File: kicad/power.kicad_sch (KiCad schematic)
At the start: 2 parts, among them J1 +5V IN

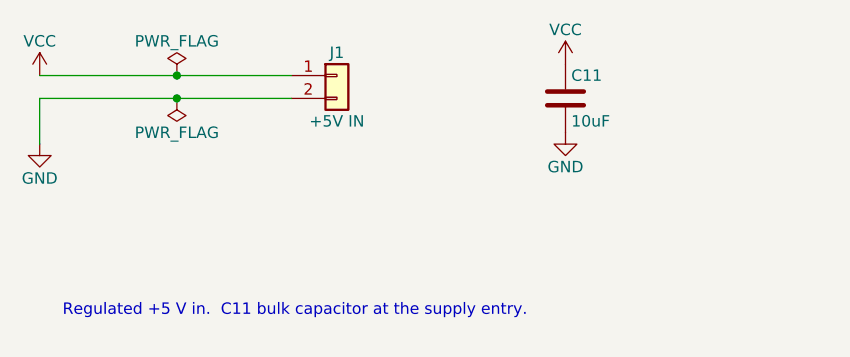
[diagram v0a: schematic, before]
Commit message: Update KiCad schematic to match the build as wired
- Remove video RAM (future expansion); GAL ~{VRAMCE} is NC and
  ~{WEGATE} goes only to the RAM
- VIA is a W65C22N6TPG-14: IRQB wired directly to ~{IRQ} (no diode)
- RDY and ~{NMI} tied directly to +5V; only reset and ~{IRQ} pull-ups
- ACIA clocked by a 1.8432 MHz DIP-8 oscillator on XTLI (EN high)
- Serial through a MAX232N to a female DB9 (pins 2, 3, 8, 5)
- VIA Port B drives eight LEDs with series resistors; Port A, CA/CB NC
- Drop per-chip decoupling; single 0.1uF electrolytic at the supply
- Unknown resistor values shown as '?'
- Update kicad/README.md and README.md accordingly

Co-Authored-By: Claude Opus 5.5 <noreply@anthropic.com>
Claude-Session: https://claude.ai/code/session_01GgTWzZQQJPzWrEMiSDZH6j
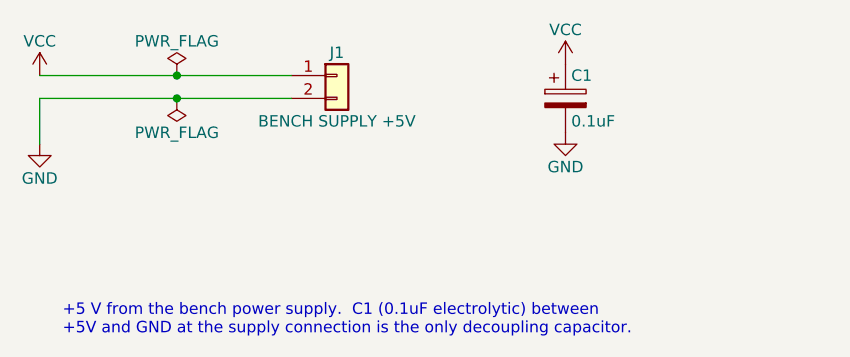
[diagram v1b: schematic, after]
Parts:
- removed C11: 10uF, symbol be6502:C
- added C1: 0.1uF, symbol be6502:C_Polarized
- J1: value +5V IN -> BENCH SUPPLY +5V
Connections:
- net GND: now also C1.2
- net VCC: now also C1.1
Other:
- note added: "+5 V from the bench power supply. C1 (0.1uF electrolytic) between +5V and GND at the supply connection is the only decoupling capacitor."
- note removed: "Regulated +5 V in. C11 bulk capacitor at the supply entry."

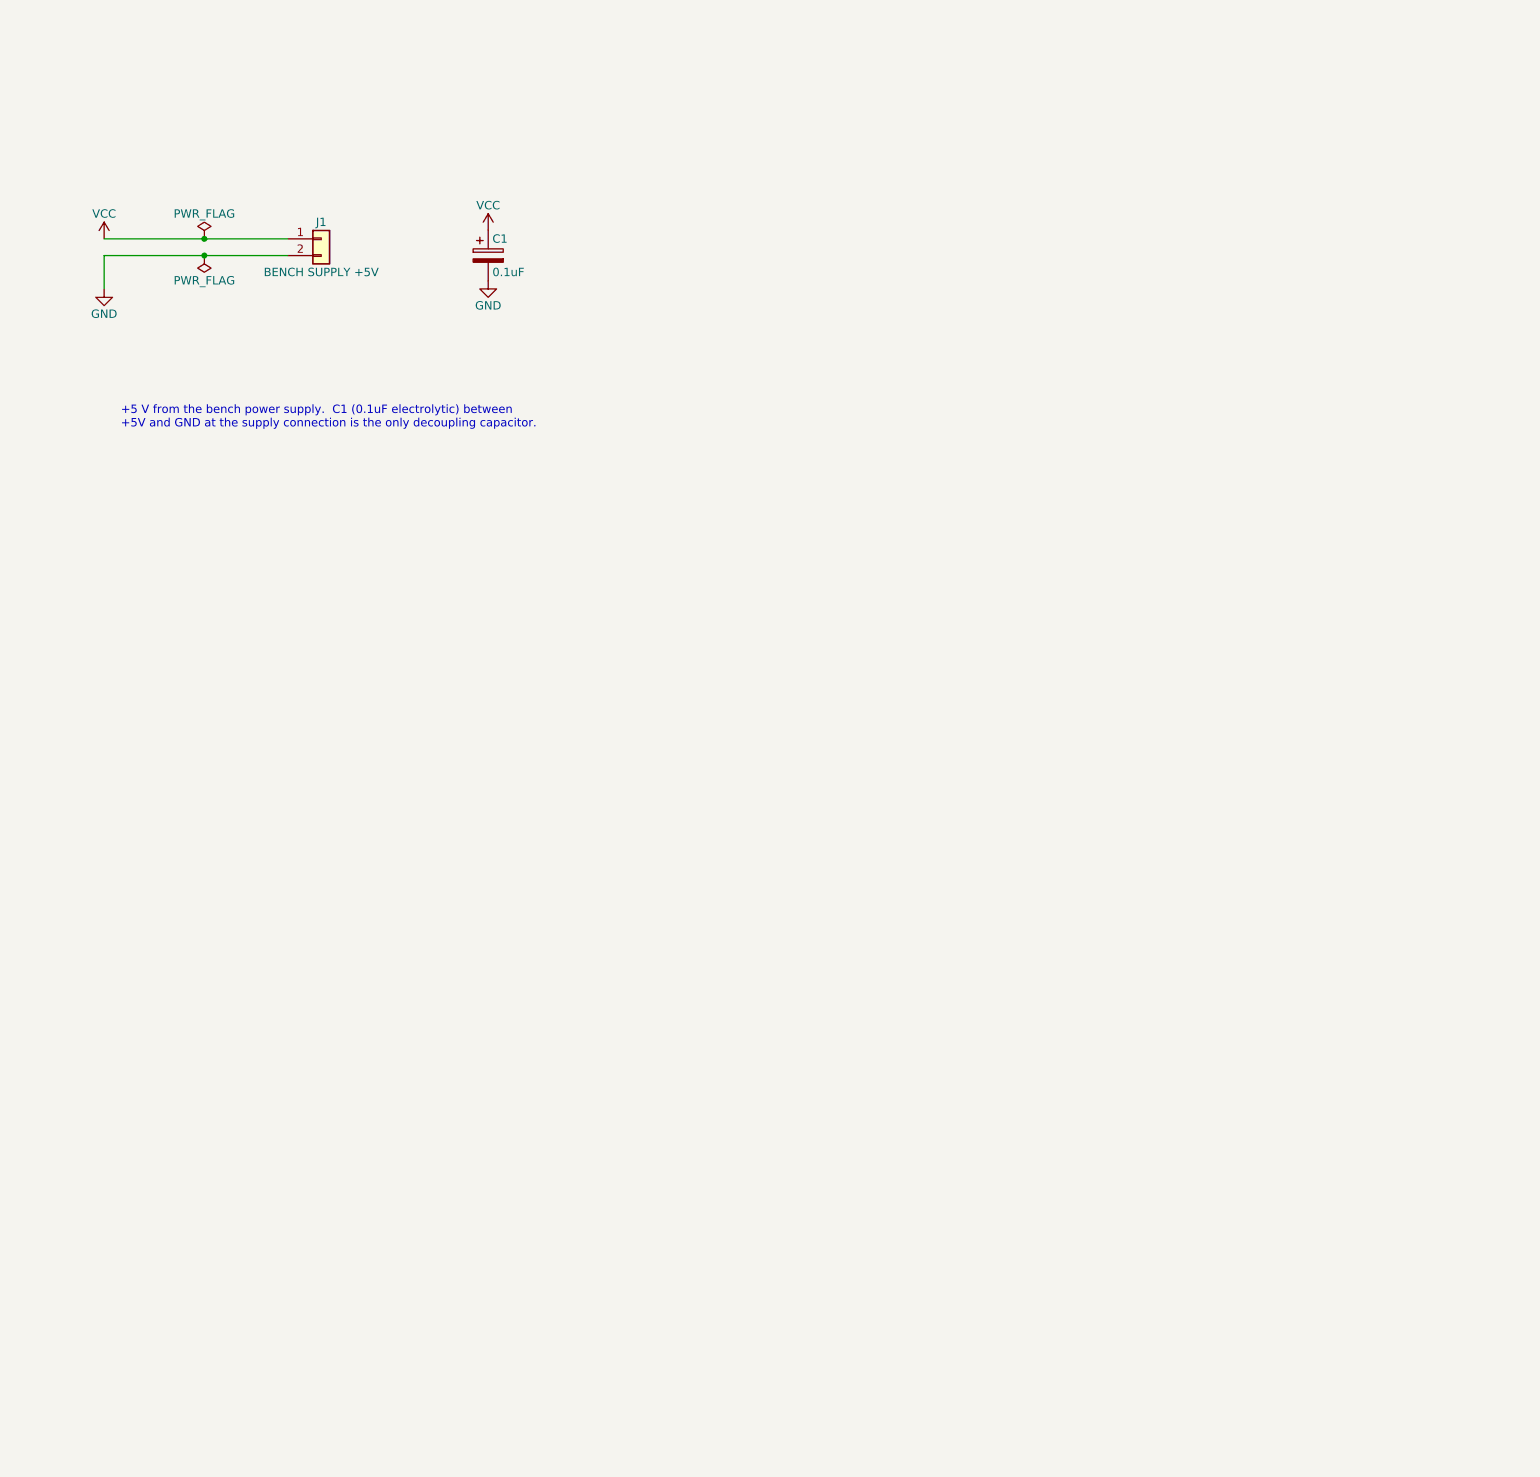
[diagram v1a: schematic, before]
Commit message: Schematic rev 2: prepare the design for a 4-layer PCB
Keeps the breadboard's parts and logic and adds what a board needs.

- RDY, NMI, ABORT and BE get 3.3k pull-ups instead of hard ties to +5V
  (RDY is bidirectional; WAI drives it low).
- VDA and VPA go to GAL pins 11 and 13. New pld/decode03.pld (816DEC03)
  qualifies /IOSEL with VDA + VPA so internal-operation cycles cannot
  read and clear ACIA/VIA registers. decode.pld (816DEC02) stays for the
  breadboard.
- PHI2 from the GAL can be routed through a 74ACT08 buffer via JP2
  (default: direct, as built). Timing in decode03.pld NOTE 8.
- Clock source jumper JP1 and external clock header J5.
- New power sheet: USB-C (power only) or bench terminal via JP4, power
  switch, polyfuse, P-FET reverse-polarity protection, 47uF bulk, power
  LED, and 100nF decoupling per package.
- New expansion sheet: 2x30 bus header (address, latched bank byte,
  data, control, spare I/O slots), 2x12 VIA header, LED disconnect
  jumper, test points, mounting holes.
- Footprints on every part; socket footprints for all ICs.

ERC (KiCad 9.0.4 kicad-cli): 0 errors, 0 warnings. Both PLD files
assemble with Galette 0.3.0.

Co-Authored-By: Claude Opus 5.5 <noreply@anthropic.com>
Claude-Session: https://claude.ai/code/session_01WF6ESyzfg6uQED2DRD2W4Z
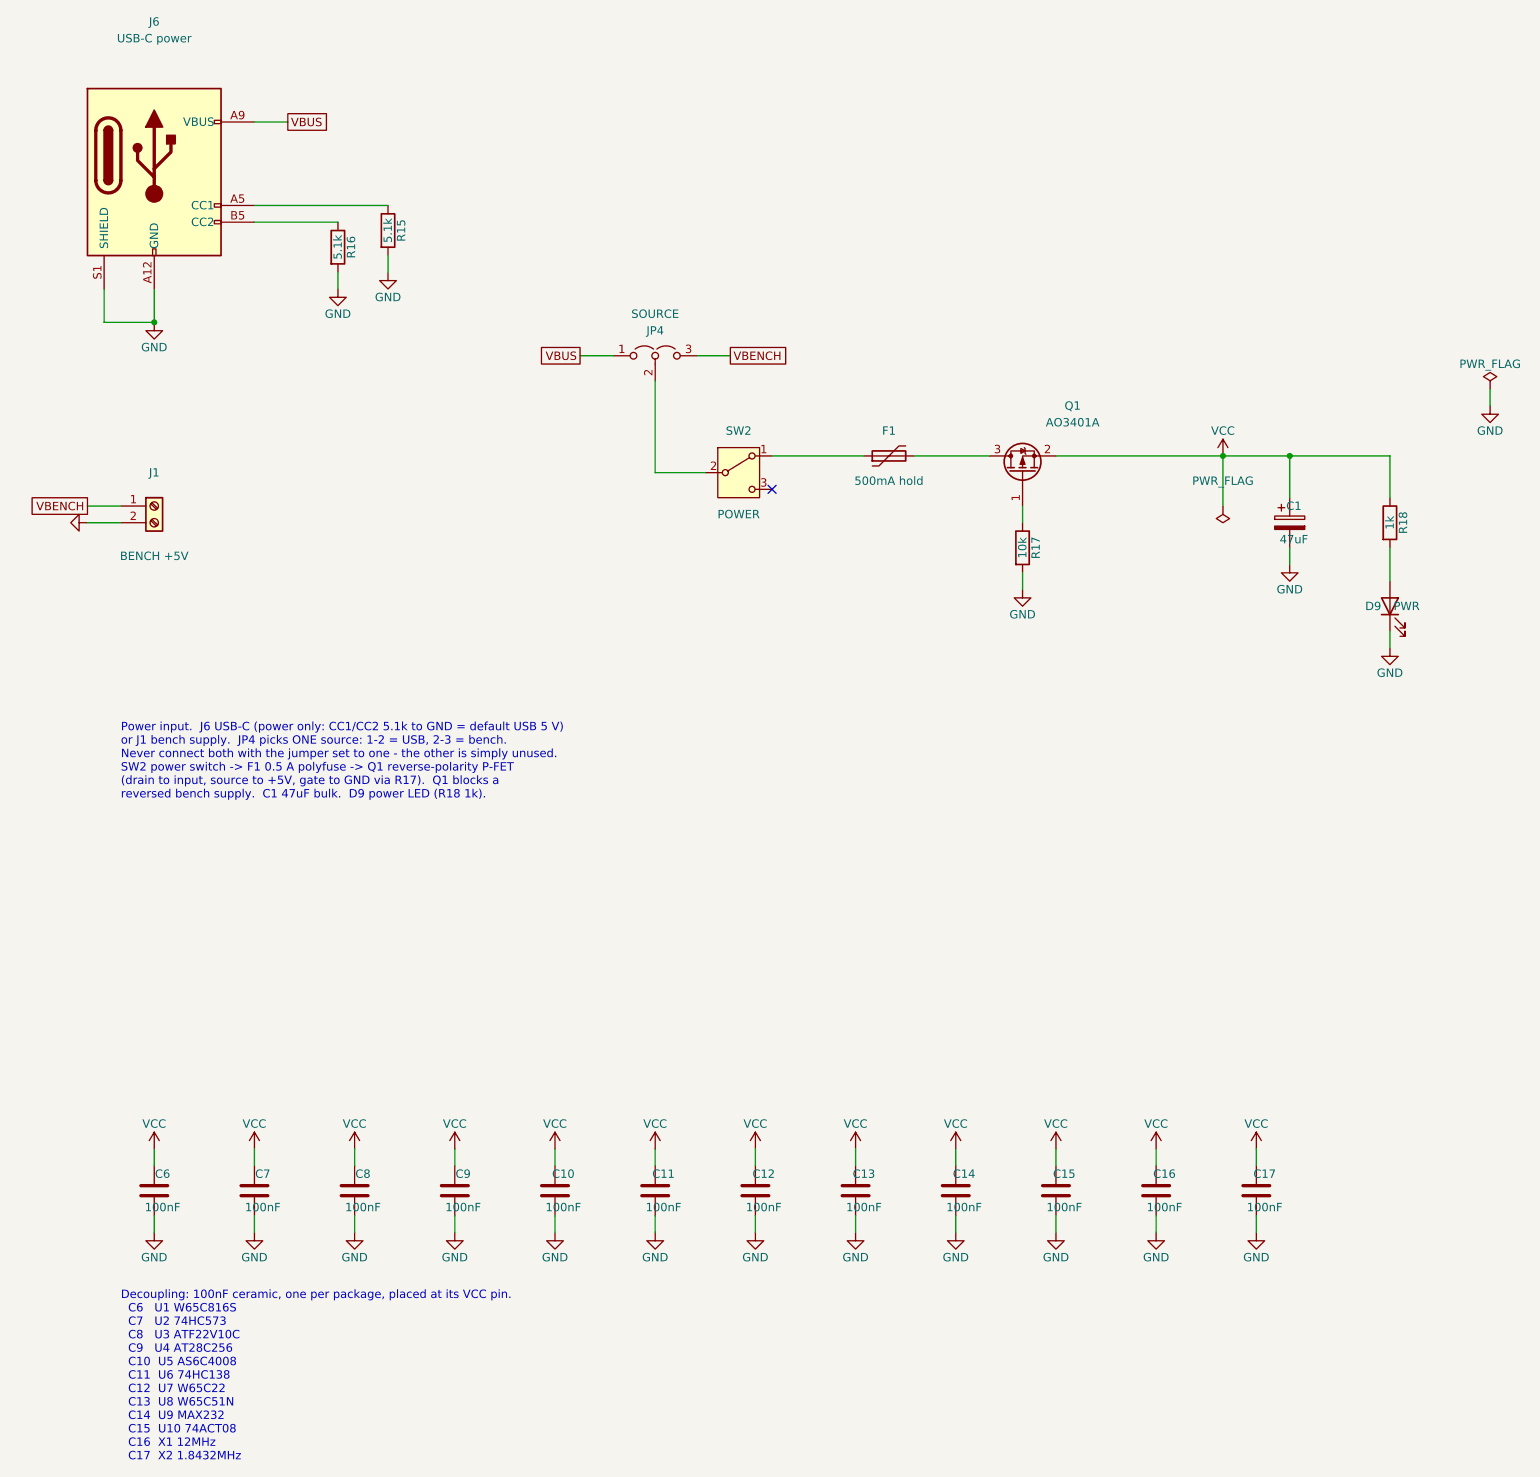
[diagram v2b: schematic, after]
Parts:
- removed J1: BENCH SUPPLY +5V, symbol be6502:Conn_01x02
- added C10, C11, C12, C13, C14, C15, C16, C17, C6, C7, C8, C9: 100nF, Capacitor_THT:C_Disc_D3.0mm_W1.6mm_P2.50mm, symbol be6502:C
- added D9: PWR, LED_THT:LED_D3.0mm, symbol be6502:LED
- added F1: 500mA hold, Fuse:Fuse_Bourns_MF-RHT050, symbol be6502:Polyfuse
- added J1: BENCH +5V, TerminalBlock_Phoenix:TerminalBlock_Phoenix_MKDS-1,5-2_1x02_P5.00mm_Horizontal, symbol be6502:Screw_Terminal_01x02
- added J6: USB-C power, Connector_USB:USB_C_Receptacle_GCT_USB4125-xx-x_6P_TopMnt_Horizontal, symbol be6502:USB_C_Receptacle_PowerOnly_6P
- added JP4: SOURCE, Connector_PinHeader_2.54mm:PinHeader_1x03_P2.54mm_Vertical, symbol be6502:Jumper_3_Open
- added Q1: AO3401A, Package_TO_SOT_SMD:SOT-23, symbol be6502:Q_PMOS_GSD
- added R15, R16: 5.1k, Resistor_THT:R_Axial_DIN0207_L6.3mm_D2.5mm_P7.62mm_Horizontal, symbol be6502:R
- added R17: 10k, Resistor_THT:R_Axial_DIN0207_L6.3mm_D2.5mm_P7.62mm_Horizontal, symbol be6502:R
- added R18: 1k, Resistor_THT:R_Axial_DIN0207_L6.3mm_D2.5mm_P7.62mm_Horizontal, symbol be6502:R
- added SW2: POWER, Button_Switch_THT:SW_Slide_SPDT_Straight_CK_OS102011MS2Q, symbol be6502:SW_SPDT
- C1: value 0.1uF -> 47uF; footprint (none) -> Capacitor_THT:CP_Radial_D6.3mm_P2.50mm
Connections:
- net GND: now also C10.2, C11.2, C12.2, C13.2, C14.2, C15.2, C16.2, C17.2, C6.2, C7.2, C8.2, C9.2, D9.1 (K), J1.2 (Pin_2), J6.A12 (GND), J6.B12 (GND), J6.S1 (SHIELD), R15.2, R16.2, R17.2
- net VCC: now also C10.1, C11.1, C12.1, C13.1, C14.1, C15.1, C16.1, C17.1, C6.1, C7.1, C8.1, C9.1, Q1.2 (S), R18.1
- new net: J6.B5 (CC2), R16.1
- new net: JP4.2 (C), SW2.2 (B)
- new net: D9.2 (A), R18.2
- new net: J6.A5 (CC1), R15.1
- new net: Q1.1 (G), R17.1
- new net: F1.1, SW2.1 (A)
- new net: F1.2, Q1.3 (D)
- new net VBENCH: J1.1 (Pin_1), JP4.3 (B)
- new net VBUS: J6.A9 (VBUS), J6.B9 (VBUS), JP4.1 (A)
- no-connect marks 0 -> 1
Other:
- note added: "Decoupling: 100nF ceramic, one per package, placed at its VCC pin. C6 U1 W65C816S C7 U2 74HC573 C8 U3 ATF22V10C C9 U4 AT28C256 C10 U5 AS6C4008 C11 U6 74HC138 C12 U7 W65C22 C13 U8 W65C51N C14 U9 MAX232 C15 U10 74ACT08 C16 X1 12MHz C17 X2 1.8432MHz"
- note added: "Power input. J6 USB-C (power only: CC1/CC2 5.1k to GND = default USB 5 V) or J1 bench supply. JP4 picks ONE source: 1-2 = USB, 2-3 = bench. Never connect both with the jumper set to one - the other is simply unused. SW2 power switch -> F1 0.5 A polyfuse -> Q1 reverse-polarity P-FET (drain to input, source to +5V, gate to GND via R17). Q1 blocks a reversed bench supply. C1 47uF bulk. D9 power LED 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"
- note removed: "+5 V from the bench power supply. C1 (0.1uF electrolytic) between +5V and GND at the supply connection is the only decoupling capacitor."
- title: Power -> Power: input, protection, decoupling
